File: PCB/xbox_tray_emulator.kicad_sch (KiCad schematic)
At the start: 4 parts, among them J1 to Xbox, U1 ATtiny13A-S

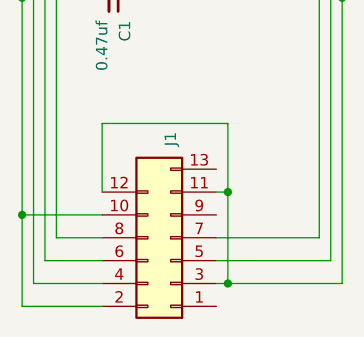
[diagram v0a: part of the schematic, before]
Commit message: reduce sleep current from 200uA to 50uA
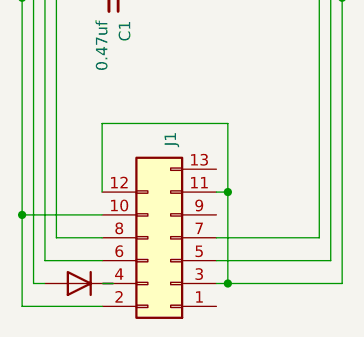
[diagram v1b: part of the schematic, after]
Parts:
- added D1: 1N4148, Diode_SMD:D_0805_2012Metric_Pad1.15x1.40mm_HandSolder, symbol Device:D
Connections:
- net at J1.4 (Pin_4): now also D1.1 (K); no longer U1.5 (PB0)
- new net: D1.2 (A), U1.5 (PB0)
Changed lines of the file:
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@@
+    (stroke (width 0) (type default) (color 0 0 0 0))
+  )
+  (wire (pts (xy 154.94 139.7) (xy 156.21 139.7))
     (stroke (width 0) (type default) (color 0 0 0 0))
   )
@@
     (stroke (width 0) (type default) (color 0 0 0 0))
   )
+  (wire (pts (xy 162.56 139.7) (xy 163.83 139.7))
+    (stroke (width 0) (type default) (color 0 0 0 0))
+  )
   (wire (pts (xy 153.67 132.08) (xy 153.67 142.24))
     (stroke (width 0) (type default) (color 0 0 0 0))
@@
   )
   (wire (pts (xy 176.53 139.7) (xy 175.26 139.7))
-    (stroke (width 0) (type default) (color 0 0 0 0))
-  )
-  (wire (pts (xy 154.94 139.7) (xy 162.56 139.7))
     (stroke (width 0) (type default) (color 0 0 0 0))
   )
@@
     (pin "2")
   )
+  (symbol (lib_id "Device:D") (at 160.02 139.7 180) (unit 1)
+    (in_bom yes) (on_board yes) (fields_autoplaced)
+    (property "Reference" "D1" (id 0) (at 160.02 133.35 0)
+      (effects (font (size 1.27 1.27)) hide)
+    )
+    (property "Value" "1N4148" (id 1) (at 160.02 135.89 0)
+      (effects (font (size 1.27 1.27)) hide)
+    )
+    (property "Footprint" "Diode_SMD:D_0805_2012Metric_Pad1.15x1.40mm_HandSolder" (id 2) (at 160.02 139.7 0)
+      (effects (font (size 1.27 1.27)) hide)
+    )
+    (property "Datasheet" "~" (id 3) (at 160.02 139.7 0)
+      (effects (font (size 1.27 1.27)) hide)
+    )
+    (pin "1")
+    (pin "2")
+  )
   (symbol (lib_id "MCU_Microchip_ATtiny:ATtiny13A-S") (at 170.18 74.93 90) (mirror x) (unit 1)
     (in_bom yes) (on_board yes) (fields_autoplaced)
@@
       (reference "C1") (unit 1) (value "0.47uf") (footprint "Capacitor_SMD:C_0805_2012Metric_Pad1.18x1.45mm_HandSolder")
     )
+    (path "/cd74d053-e62a-45a3-9f24-631862f85655"
+      (reference "D1") (unit 1) (value "1N4148") (footprint "Diode_SMD:D_0805_2012Metric_Pad1.15x1.40mm_HandSolder")
+    )
     (path "/47075e9c-a9f4-44e8-9794-9a28acff27bb"

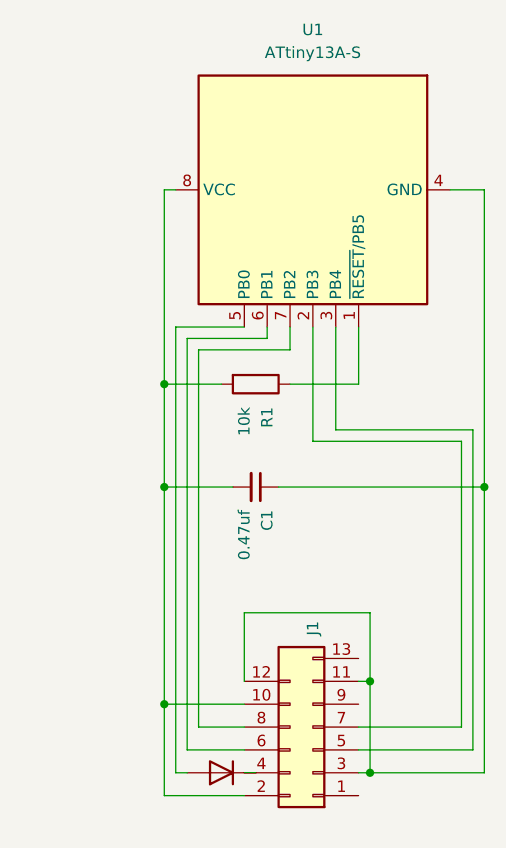
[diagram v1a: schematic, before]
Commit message: Xbox DVD logic levels are 3.3v, a 3.3v regulator was added to the PCB so the ATtiny13a will output and accept 3.3v logic. ATtiny13a sleep current draw is now a fration of a uA. modify tray open sequence to closer approximate a real DVD drive.
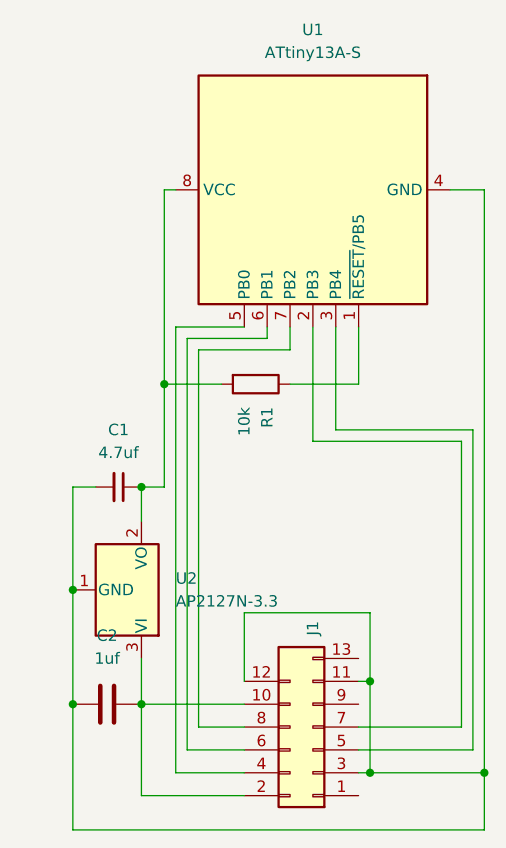
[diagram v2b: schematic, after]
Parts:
- removed D1: 1N4148, Diode_SMD:D_0805_2012Metric_Pad1.15x1.40mm_HandSolder, symbol Device:D
- added C2: 1uf, Capacitor_SMD:C_0805_2012Metric_Pad1.18x1.45mm_HandSolder, symbol Device:C
- added U2: AP2127N-3.3, Package_TO_SOT_SMD:SOT-23, symbol Regulator_Linear:AP2127N-3.3
- C1: value 0.47uf -> 4.7uf
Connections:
- net at J1.11 (Pin_11), J1.12 (Pin_12), J1.3 (Pin_3)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: now also C1.2, C2.2, U2.1 (GND); no longer C1.1
- net at J1.4 (Pin_4): now also U1.5 (PB0)
- new net: C1.1, R1.2, U1.8 (VCC), U2.2 (VO)
- new net: C2.1, J1.10 (Pin_10), J1.2 (Pin_2), U2.3 (VI)
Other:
- moved on the sheet: C1
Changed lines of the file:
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@@
   (junction (at 176.53 129.54) (diameter 0) (color 0 0 0 0)
   )
+  (junction (at 143.51 132.08) (diameter 0) (color 0 0 0 0)
+  )
+  (junction (at 151.13 132.08) (diameter 0) (color 0 0 0 0)
+  )
+  (junction (at 189.23 139.7) (diameter 0) (color 0 0 0 0)
+  )
+  (junction (at 151.13 107.95) (diameter 0) (color 0 0 0 0)
+  )
   (junction (at 176.53 139.7) (diameter 0) (color 0 0 0 0)
   )
   (junction (at 153.67 96.52) (diameter 0) (color 0 0 0 0)
   )
-  (junction (at 189.23 107.95) (diameter 0) (color 0 0 0 0)
-  )
-  (junction (at 153.67 107.95) (diameter 0) (color 0 0 0 0)
-  )
-  (junction (at 153.67 132.08) (diameter 0) (color 0 0 0 0)
+  (junction (at 143.51 119.38) (diameter 0) (color 0 0 0 0)
   )
   (wire (pts (xy 186.69 102.87) (xy 186.69 134.62))
     (stroke (width 0) (type default) (color 0 0 0 0))
   )
-  (wire (pts (xy 162.56 132.08) (xy 153.67 132.08))
-    (stroke (width 0) (type default) (color 0 0 0 0))
-  )
-  (wire (pts (xy 154.94 139.7) (xy 156.21 139.7))
-    (stroke (width 0) (type default) (color 0 0 0 0))
-  )
-  (wire (pts (xy 153.67 142.24) (xy 162.56 142.24))
-    (stroke (width 0) (type default) (color 0 0 0 0))
-  )
-  (wire (pts (xy 162.56 139.7) (xy 163.83 139.7))
-    (stroke (width 0) (type default) (color 0 0 0 0))
-  )
-  (wire (pts (xy 153.67 132.08) (xy 153.67 142.24))
+  (wire (pts (xy 143.51 146.05) (xy 189.23 146.05))
+    (stroke (width 0) (type default) (color 0 0 0 0))
+  )
+  (wire (pts (xy 151.13 127) (xy 151.13 132.08))
+    (stroke (width 0) (type default) (color 0 0 0 0))
+  )
+  (wire (pts (xy 189.23 146.05) (xy 189.23 139.7))
+    (stroke (width 0) (type default) (color 0 0 0 0))
+  )
+  (wire (pts (xy 154.94 139.7) (xy 162.56 139.7))
+    (stroke (width 0) (type default) (color 0 0 0 0))
+  )
+  (wire (pts (xy 143.51 119.38) (xy 143.51 132.08))
     (stroke (width 0) (type default) (color 0 0 0 0))
   )
@@
     (stroke (width 0) (type default) (color 0 0 0 0))
   )
+  (wire (pts (xy 143.51 107.95) (xy 146.05 107.95))
+    (stroke (width 0) (type default) (color 0 0 0 0))
+  )
   (wire (pts (xy 187.96 137.16) (xy 175.26 137.16))
     (stroke (width 0) (type default) (color 0 0 0 0))
@@
     (stroke (width 0) (type default) (color 0 0 0 0))
   )
-  (wire (pts (xy 189.23 107.95) (xy 189.23 139.7))
+  (wire (pts (xy 189.23 74.93) (xy 189.23 139.7))
     (stroke (width 0) (type default) (color 0 0 0 0))
   )
@@
     (stroke (width 0) (type default) (color 0 0 0 0))
   )
+  (wire (pts (xy 143.51 119.38) (xy 143.51 107.95))
+    (stroke (width 0) (type default) (color 0 0 0 0))
+  )
   (wire (pts (xy 176.53 121.92) (xy 162.56 121.92))
     (stroke (width 0) (type default) (color 0 0 0 0))
@@
     (stroke (width 0) (type default) (color 0 0 0 0))
   )
+  (wire (pts (xy 151.13 142.24) (xy 162.56 142.24))
+    (stroke (width 0) (type default) (color 0 0 0 0))
+  )
+  (wire (pts (xy 162.56 132.08) (xy 151.13 132.08))
+    (stroke (width 0) (type default) (color 0 0 0 0))
+  )
   (wire (pts (xy 162.56 90.17) (xy 154.94 90.17))
     (stroke (width 0) (type default) (color 0 0 0 0))
@@
     (stroke (width 0) (type default) (color 0 0 0 0))
   )
-  (wire (pts (xy 161.29 107.95) (xy 153.67 107.95))
-    (stroke (width 0) (type default) (color 0 0 0 0))
-  )
   (wire (pts (xy 167.64 92.71) (xy 157.48 92.71))
     (stroke (width 0) (type default) (color 0 0 0 0))
   )
+  (wire (pts (xy 151.13 107.95) (xy 151.13 111.76))
+    (stroke (width 0) (type default) (color 0 0 0 0))
+  )
   (wire (pts (xy 162.56 121.92) (xy 162.56 129.54))
     (stroke (width 0) (type default) (color 0 0 0 0))
@@
     (stroke (width 0) (type default) (color 0 0 0 0))
   )
-  (wire (pts (xy 189.23 74.93) (xy 189.23 107.95))
-    (stroke (width 0) (type default) (color 0 0 0 0))
-  )
   (wire (pts (xy 186.69 134.62) (xy 175.26 134.62))
     (stroke (width 0) (type default) (color 0 0 0 0))
   )
-  (wire (pts (xy 153.67 107.95) (xy 153.67 132.08))
+  (wire (pts (xy 151.13 132.08) (xy 151.13 142.24))
     (stroke (width 0) (type default) (color 0 0 0 0))
   )
@@
     (stroke (width 0) (type default) (color 0 0 0 0))
   )
+  (wire (pts (xy 153.67 107.95) (xy 151.13 107.95))
+    (stroke (width 0) (type default) (color 0 0 0 0))
+  )
   (wire (pts (xy 170.18 102.87) (xy 186.69 102.87))
     (stroke (width 0) (type default) (color 0 0 0 0))
   )
-  (wire (pts (xy 166.37 107.95) (xy 189.23 107.95))
-    (stroke (width 0) (type default) (color 0 0 0 0))
-  )
   (wire (pts (xy 172.72 101.6) (xy 187.96 101.6))
     (stroke (width 0) (type default) (color 0 0 0 0))
@@
     (stroke (width 0) (type default) (color 0 0 0 0))
   )
+  (wire (pts (xy 143.51 132.08) (xy 143.51 146.05))
+    (stroke (width 0) (type default) (color 0 0 0 0))
+  )
   (wire (pts (xy 189.23 139.7) (xy 176.53 139.7))
     (stroke (width 0) (type default) (color 0 0 0 0))
@@
   (wire (pts (xy 156.21 137.16) (xy 162.56 137.16))
     (stroke (width 0) (type default) (color 0 0 0 0))
+  )
+  (symbol (lib_id "Regulator_Linear:AP2127N-3.3") (at 151.13 119.38 270) (mirror x) (unit 1)
+    (in_bom yes) (on_board yes) (fields_autoplaced)
+    (property "Reference" "U2" (id 0) (at 154.94 118.1099 90)
+      (effects (font (size 1.27 1.27)) (justify left))
+    )
+    (property "Value" "AP2127N-3.3" (id 1) (at 154.94 120.6499 90)
+      (effects (font (size 1.27 1.27)) (justify left))
+    )
+    (property "Footprint" "Package_TO_SOT_SMD:SOT-23" (id 2) (at 156.845 119.38 0)
+      (effects (font (size 1.27 1.27) italic) hide)
+    )
+    (property "Datasheet" "https://www.diodes.com/assets/Datasheets/AP2127.pdf" (id 3) (at 151.13 119.38 0)
+      (effects (font (size 1.27 1.27)) hide)
+    )
+    (pin "1")
+    (pin "2")
+    (pin "3")
+  )
+  (symbol (lib_id "Device:C") (at 147.32 132.08 270) (unit 1)
+    (in_bom yes) (on_board yes) (fields_autoplaced)
+    (property "Reference" "C2" (id 0) (at 147.32 124.46 90))
+    (property "Value" "1uf" (id 1) (at 147.32 127 90))
+    (property "Footprint" "Capacitor_SMD:C_0805_2012Metric_Pad1.18x1.45mm_HandSolder" (id 2) (at 143.51 133.0452 0)
+      (effects (font (size 1.27 1.27)) hide)
+    )
+    (property "Datasheet" "~" (id 3) (at 147.32 132.08 0)
+      (effects (font (size 1.27 1.27)) hide)
+    )
+    (pin "1")
+    (pin "2")
   )
   (symbol (lib_id "Device:R") (at 163.83 96.52 270) (unit 1)
@@
     (pin "9")
   )
-  (symbol (lib_id "Device:C_Small") (at 163.83 107.95 270) (unit 1)
-    (in_bom yes) (on_board yes) (fields_autoplaced)
-    (property "Reference" "C1" (id 0) (at 165.0938 110.49 0)
-      (effects (font (size 1.27 1.27)) (justify left))
-    )
-    (property "Value" "0.47uf" (id 1) (at 162.5538 110.49 0)
-      (effects (font (size 1.27 1.27)) (justify left))
-    )
-    (property "Footprint" "Capacitor_SMD:C_0805_2012Metric_Pad1.18x1.45mm_HandSolder" (id 2) (at 163.83 107.95 0)
-      (effects (font (size 1.27 1.27)) hide)
-    )
-    (property "Datasheet" "~" (id 3) (at 163.83 107.95 0)
-      (effects (font (size 1.27 1.27)) hide)
-    )
-    (pin "1")
-    (pin "2")
-  )
-  (symbol (lib_id "Device:D") (at 160.02 139.7 180) (unit 1)
-    (in_bom yes) (on_board yes) (fields_autoplaced)
-    (property "Reference" "D1" (id 0) (at 160.02 133.35 0)
-      (effects (font (size 1.27 1.27)) hide)
-    )
-    (property "Value" "1N4148" (id 1) (at 160.02 135.89 0)
-      (effects (font (size 1.27 1.27)) hide)
-    )
-    (property "Footprint" "Diode_SMD:D_0805_2012Metric_Pad1.15x1.40mm_HandSolder" (id 2) (at 160.02 139.7 0)
-      (effects (font (size 1.27 1.27)) hide)
-    )
-    (property "Datasheet" "~" (id 3) (at 160.02 139.7 0)
+  (symbol (lib_id "Device:C_Small") (at 148.59 107.95 270) (unit 1)
+    (in_bom yes) (on_board yes) (fields_autoplaced)
+    (property "Reference" "C1" (id 0) (at 148.5836 101.6 90))
+    (property "Value" "4.7uf" (id 1) (at 148.5836 104.14 90))
+    (property "Footprint" "Capacitor_SMD:C_0805_2012Metric_Pad1.18x1.45mm_HandSolder" (id 2) (at 148.59 107.95 0)
+      (effects (font (size 1.27 1.27)) hide)
+    )
+    (property "Datasheet" "~" (id 3) (at 148.59 107.95 0)
       (effects (font (size 1.27 1.27)) hide)
     )
@@
   (symbol_instances
     (path "/689a08ee-6ac4-44dd-84ed-a3f9f79b5960"
-      (reference "C1") (unit 1) (value "0.47uf") (footprint "Capacitor_SMD:C_0805_2012Metric_Pad1.18x1.45mm_HandSolder")
-    )
-    (path "/cd74d053-e62a-45a3-9f24-631862f85655"
-      (reference "D1") (unit 1) (value "1N4148") (footprint "Diode_SMD:D_0805_2012Metric_Pad1.15x1.40mm_HandSolder")
+      (reference "C1") (unit 1) (value "4.7uf") (footprint "Capacitor_SMD:C_0805_2012Metric_Pad1.18x1.45mm_HandSolder")
+    )
+    (path "/18fae36d-0022-4cd3-a697-522a84454a34"
+      (reference "C2") (unit 1) (value "1uf") (footprint "Capacitor_SMD:C_0805_2012Metric_Pad1.18x1.45mm_HandSolder")
     )
     (path "/47075e9c-a9f4-44e8-9794-9a28acff27bb"
@@
       (reference "U1") (unit 1) (value "ATtiny13A-S") (footprint "Package_SO:SOIC-8W_5.3x5.3mm_P1.27mm")
     )
-  )
+    (path "/08911ef2-2085-431b-a5d1-57624067f1b3"
+      (reference "U2") (unit 1) (value "AP2127N-3.3") (footprint "Package_TO_SOT_SMD:SOT-23")
+    )
+  )

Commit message: add ground fill
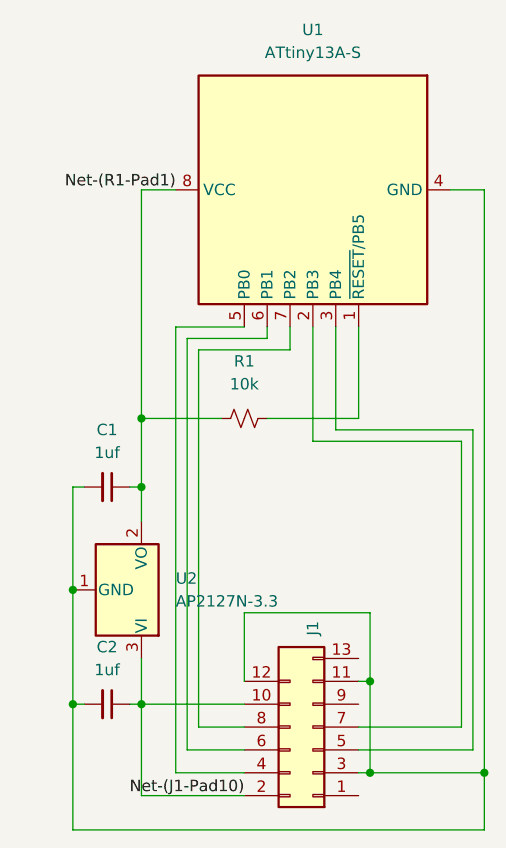
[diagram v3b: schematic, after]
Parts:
- removed C2: 1uf, Capacitor_SMD:C_0805_2012Metric_Pad1.18x1.45mm_HandSolder, symbol Device:C
- removed R1: 10k, Resistor_SMD:R_0805_2012Metric_Pad1.20x1.40mm_HandSolder, symbol Device:R
- added C2: 1uf, Capacitor_SMD:C_0805_2012Metric_Pad1.18x1.45mm_HandSolder, symbol Device:C_Small
- added R1: 10k, Resistor_SMD:R_0805_2012Metric_Pad1.20x1.40mm_HandSolder, symbol Device:R_Small_US
- C1: value 4.7uf -> 1uf
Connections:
- net at C1.2, J1.11 (Pin_11), J1.12 (Pin_12)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: now also C2.2
- net Net-(R1-Pad1): now reaches C1.1, U1.8 (VCC), U2.2 (VO)
- net Net-(R1-Pad1): now also R1.1
- net Net-(J1-Pad10): now reaches J1.10 (Pin_10), J1.2 (Pin_2), U2.3 (VI)
- net Net-(J1-Pad10): now also C2.1
- net at U1.1 (~{RESET}/PB5): now also R1.2
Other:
- moved on the sheet: C1
